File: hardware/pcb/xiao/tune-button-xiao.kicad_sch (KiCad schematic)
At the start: 14 parts, among them J1 XIAO left, J2 XIAO right, J3 LiPo, J4 to XIAO BAT, SW1 MX switch, SW2 MX switch, SW3 MX switch, SW4 MX switch

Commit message: C3 PCB: JLC Basic/Preferred parts where a drop-in exists, LCSC numbers, JLC BOM and CPL
TP4054 for MCP73831, XC6206 for MCP1700 and SRV05-4 for USBLC6-2SC6, each with the same footprint
and pinout. Every assembled part carries its LCSC number; the build writes JLC-format BOM and
placement files listing only those parts. Only the module, USB-C and JST sockets remain Extended.
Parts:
- C1: LCSC (none) -> C14663
- D2: LCSC (none) -> C2286
- R1, R2: LCSC (none) -> C22961
- R3: LCSC (none) -> C21190
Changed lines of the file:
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@@
+			(effects (font (size 1.27 1.27)) (hide yes))
+		)
+		(property "LCSC" "C14663"
+			(at 40.64 187.96 0)
 			(effects (font (size 1.27 1.27)) (hide yes))
 		)
@@
 			(effects (font (size 1.27 1.27)) (hide yes))
 		)
+		(property "LCSC" "C2286"
+			(at 40.64 233.68 0)
+			(effects (font (size 1.27 1.27)) (hide yes))
+		)
 		(pin "1")
 		(pin "2")
@@
 			(effects (font (size 1.27 1.27)) (hide yes))
 		)
+		(property "LCSC" "C22961"
+			(at 40.64 264.16 0)
+			(effects (font (size 1.27 1.27)) (hide yes))
+		)
 		(pin "1")
 		(pin "2")
@@
 			(effects (font (size 1.27 1.27)) (hide yes))
 		)
+		(property "LCSC" "C22961"
+			(at 116.84 71.12 0)
+			(effects (font (size 1.27 1.27)) (hide yes))
+		)
 		(pin "1")
 		(pin "2")
@@
 			(effects (font (size 1.27 1.27)) (hide yes))
 		)
+		(property "LCSC" "C21190"
+			(at 116.84 96.52 0)
+			(effects (font (size 1.27 1.27)) (hide yes))
+		)

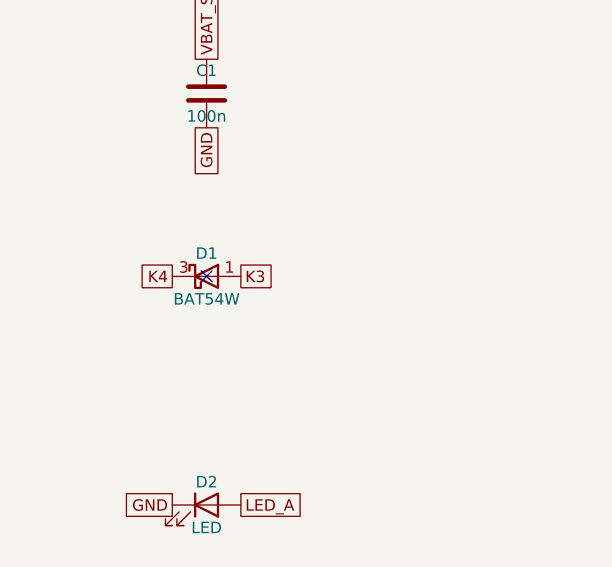
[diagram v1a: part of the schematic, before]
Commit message: pcb: fixes from the fourth simulation pass
- C3: R13/R14 (plug-in damping) are 1206, not 0603. Each takes a ~35 W,
  ~50 uJ pulse per plug-in from a stiff source, about twice an 0603's
  repetitive pulse rating. Moved flat above U4; C1 nudged down.
- XIAO: D1 is a 1N4148WS, not a BAT54W. A Schottky's reverse leakage
  dragged K4 low while K3 was held, from about 60 C.
- R5 comment: the unplug gap is 5-8 ms, up to ~15 ms at tolerance extremes.
- wiring.md: the divider holds GPIO2 below the high threshold; it doesn't
  select the boot mode on the C3, so that is fine.
- README: the firmware pin map doesn't match either board yet, and a low
  cell sags the C3 rail on Wi-Fi-sized bursts.
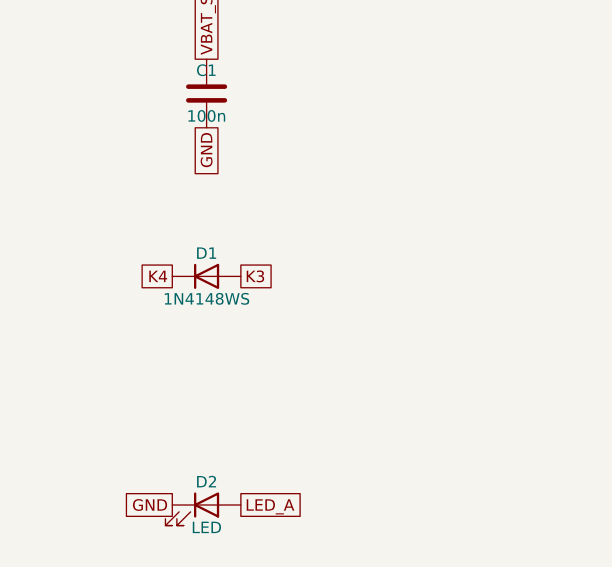
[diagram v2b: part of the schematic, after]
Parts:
- D1: value BAT54W -> 1N4148WS; footprint Package_TO_SOT_SMD:SOT-323_SC-70 -> Diode_SMD:D_SOD-323; symbol Diode:BAT54W -> Diode:1N4148WS; MPN BAT54W -> 1N4148WS
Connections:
- net K3: now also D1.2 (A); no longer D1.1 (A)
- net K4: now also D1.1 (K); no longer D1.3 (K)
- no-connect marks 8 -> 7
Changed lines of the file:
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@@
 	)
 	(symbol
-		(lib_id "Diode:BAT54W")
+		(lib_id "Diode:1N4148WS")
 		(at 40.64 198.12 0)
 		(unit 1)
@@
 			(effects (font (size 1.27 1.27)))
 		)
-		(property "Value" "BAT54W"
+		(property "Value" "1N4148WS"
 			(at 40.64 200.66 0)
 			(effects (font (size 1.27 1.27)))
 		)
-		(property "Footprint" "Package_TO_SOT_SMD:SOT-323_SC-70"
+		(property "Footprint" "Diode_SMD:D_SOD-323"
 			(at 40.64 203.2 0)
 			(effects (font (size 1.27 1.27)) (hide yes))
@@
 			(effects (font (size 1.27 1.27)) (hide yes))
 		)
-		(property "MPN" "BAT54W"
+		(property "MPN" "1N4148WS"
 			(at 40.64 205.74 0)
 			(effects (font (size 1.27 1.27)) (hide yes))
 		)
-		(pin "3")
+		(pin "1")
 		(pin "2")
-		(pin "1")
 		(instances
 			(project "tune-button-xiao"
@@
 		)
 	)
-	(no_connect (at 40.64 198.12))
 	(global_label "K3"
 		(shape passive)

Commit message: pcb: fixes from the fifth audit
- XIAO D1: LCSC C2128 (Changjing 1N4148WS, Basic), so it appears in the JLC
  BOM/CPL. Its VF max of 0.715 V at 1 mA is what the K4 press needs to read
  low at -20 C; the README says so. Hand-soldering footprint, as that board is.
- Labels: a label must be nearer its own part than any other by 0.25 mm,
  measured edge to edge (it was centre to body). C1's label passes that and
  stays beside C1; U4's, which the first try at this rule hid, is placed.
- route.py drops exactly repeated track segments from the saved board
  (removing them through pcbnew's bindings crashes it later in the run).
- variant_xiao docstring no longer says Schottky.
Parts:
- D1: footprint Diode_SMD:D_SOD-323 -> Diode_SMD:D_SOD-323_HandSoldering; LCSC (none) -> C2128
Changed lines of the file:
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@@
 			(effects (font (size 1.27 1.27)))
 		)
-		(property "Footprint" "Diode_SMD:D_SOD-323"
+		(property "Footprint" "Diode_SMD:D_SOD-323_HandSoldering"
 			(at 40.64 203.2 0)
 			(effects (font (size 1.27 1.27)) (hide yes))
@@
 			(effects (font (size 1.27 1.27)) (hide yes))
 		)
+		(property "LCSC" "C2128"
+			(at 40.64 208.28 0)
+			(effects (font (size 1.27 1.27)) (hide yes))
+		)

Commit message: pcb: one panel of all three boards for Standard PCBA; JLC fits the XIAO board's parts
panel.py builds a 146 x 72 mm KiKit panel (XIAO, C3, c3-jst, 5 mm rails left and right,
JLC tooling holes and fiducials on the rails) from the committed boards. Mouse-bite tabs
go only where no track, via or pad is within 1 mm of the edge; the pour is held back
around each, and a narrow tab gets no fillet so its bites stay inside the clear span.
It writes the panel's gerbers and JLC BOM/CPL, designators prefixed by board, each part
placed as on its own board through fab_jlc.jlc_place (now importable).

The XIAO board's battery JST, 1x7 sockets and 2-pin header get LCSC numbers, with the
rotation and centre offset JLC's footprints need for the sockets and header (checked pad
by pad against EasyEDA).
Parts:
- J1, J2: LCSC (none) -> C2932672; MPN (none) -> Kinghelm KH-2.54FH-1X7P-H8.5
- J3: LCSC (none) -> C295747
- J4: LCSC (none) -> C492401; MPN (none) -> XFCN PZ254V-11-02P
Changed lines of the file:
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@@
+			(effects (font (size 1.27 1.27)) (hide yes))
+		)
+		(property "MPN" "Kinghelm KH-2.54FH-1X7P-H8.5"
+			(at 40.64 71.12 0)
+			(effects (font (size 1.27 1.27)) (hide yes))
+		)
+		(property "LCSC" "C2932672"
+			(at 40.64 73.66 0)
 			(effects (font (size 1.27 1.27)) (hide yes))
 		)
@@
 		(property "Datasheet" ""
 			(at 40.64 96.52 0)
+			(effects (font (size 1.27 1.27)) (hide yes))
+		)
+		(property "MPN" "Kinghelm KH-2.54FH-1X7P-H8.5"
+			(at 40.64 104.14 0)
+			(effects (font (size 1.27 1.27)) (hide yes))
+		)
+		(property "LCSC" "C2932672"
+			(at 40.64 106.68 0)
 			(effects (font (size 1.27 1.27)) (hide yes))
 		)
@@
 			(effects (font (size 1.27 1.27)) (hide yes))
 		)
+		(property "LCSC" "C295747"
+			(at 40.64 132.08 0)
+			(effects (font (size 1.27 1.27)) (hide yes))
+		)
 		(pin "1")
 		(pin "2")
@@
 			(effects (font (size 1.27 1.27)) (hide yes))
 		)
+		(property "MPN" "XFCN PZ254V-11-02P"
+			(at 40.64 157.48 0)
+			(effects (font (size 1.27 1.27)) (hide yes))
+		)
+		(property "LCSC" "C492401"
+			(at 40.64 160.02 0)
+			(effects (font (size 1.27 1.27)) (hide yes))
+		)
